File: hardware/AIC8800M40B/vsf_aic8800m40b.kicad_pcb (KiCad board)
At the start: 4 copper layers, 36.8 x 57.2 mm, 86 parts, among them J1 USB_A, J2 USB_C_Receptacle_USB2.0, J3 USB_C_Receptacle_USB2.0, J4 Micro_SD_Card_Det1, J6 Conn_Coaxial, J7 Conn_Coaxial, J8 Conn_01x05, Q1 S9013, SW1 SW_Push, SW2 SW_Push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

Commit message: [hardware/aic8800m40b] update
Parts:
- L4, L5: footprint Inductor_SMD:L_2010_5025Metric -> Inductor_SMD:L_1210_3225Metric
- moved L4 0.89 mm to (216.3, 141.9)
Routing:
- net Net-(U3-SW): track 25.5 -> 9.27 mm
- net Net-(U4-SW): track 14.6 -> 24.8 mm
- net /USB5V_OUT: track 74.5 -> 73.9 mm
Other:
- board text added: "CHIP_BOOT USB_BOOT LINUX_BOOT LINUX/APP"
- board text removed: "CHIP_BOOT USB_BOOT LINUX_BOOT"

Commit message: [hardware/aic8800m40b] update footprint of L1 to be 0805
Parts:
- L1: footprint Inductor_SMD:L_0603_1608Metric -> Inductor_SMD:L_0805_2012Metric
- moved L1 0.51 mm to (226.8, 111.4)
- moved C8 0.10 mm to (229.3, 111.4), turned to -90 degrees
- moved C9 0.10 mm to (226.9, 109.9)
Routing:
- net Net-(U1-V_RF): track 17.8 -> 22.3 mm
- net GND: track 328.9 -> 324.5 mm, vias 206 -> 205
- net /V_CORE: track 10.9 -> 14.8 mm
- net /PWR_3V3: track 137.2 -> 138.8 mm
- net Net-(U1-SW): track 8.21 -> 8.88 mm
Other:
- board text added: "CLK"
- board text added: "DIO"
- board text added: "GND"
- board text added: "RST"
- board text added: "VCC"

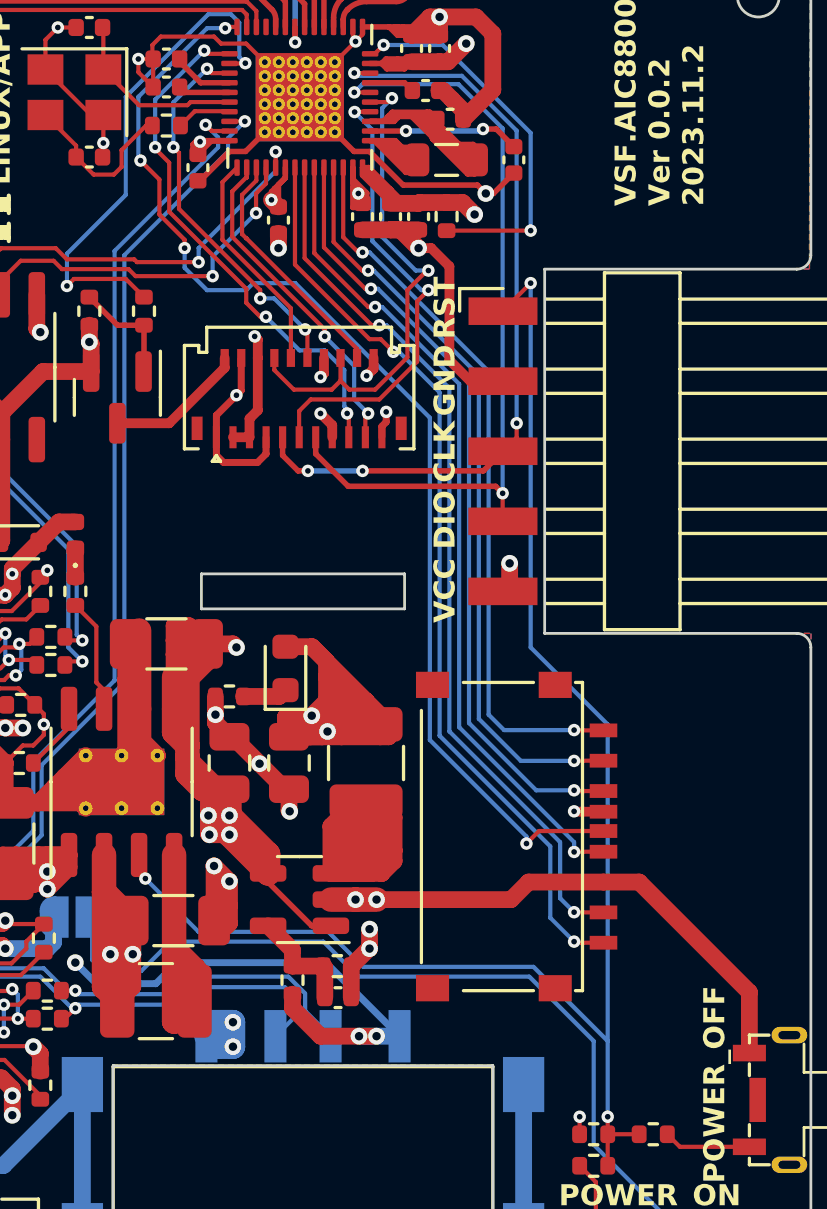
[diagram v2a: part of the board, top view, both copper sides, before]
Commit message: [hardware/aic8800m40b] add test points
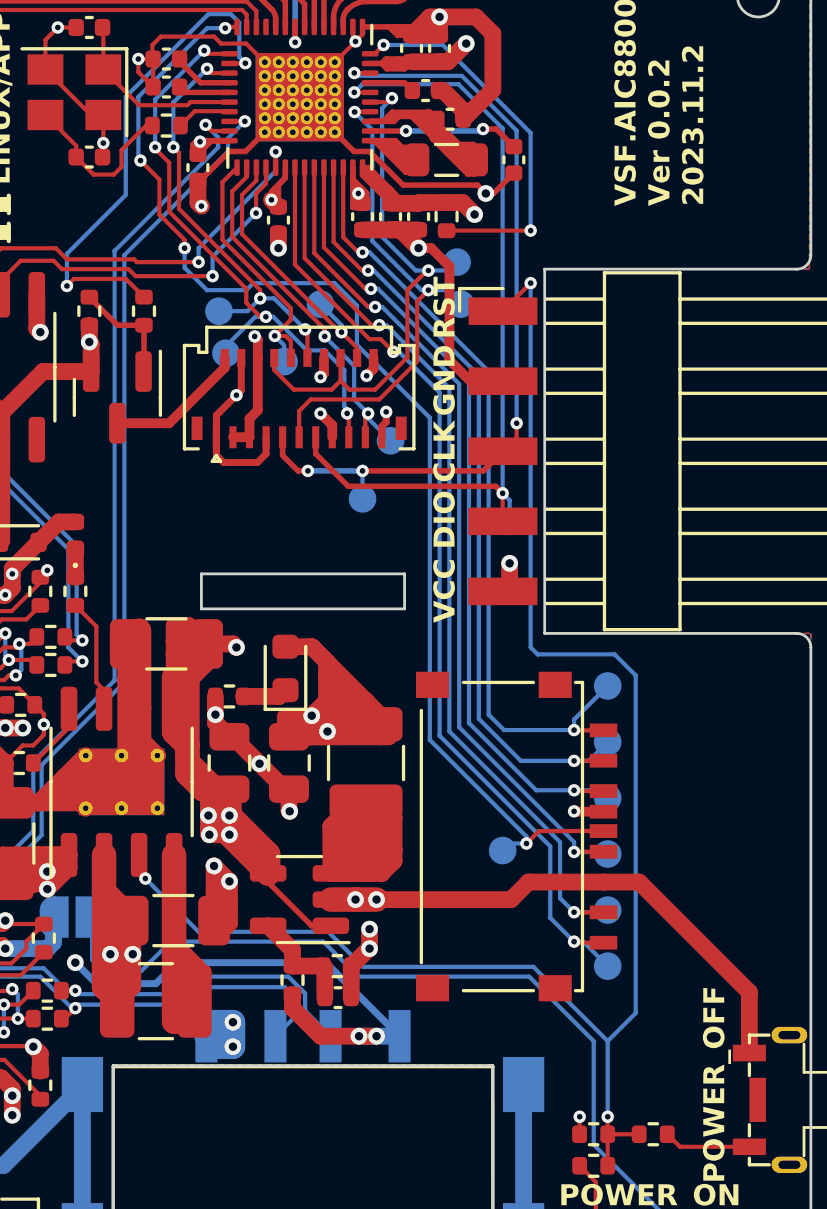
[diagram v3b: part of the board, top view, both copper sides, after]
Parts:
- added TP1: TestPoint, TestPoint:TestPoint_Pad_D1.0mm, B.Cu at (228.9, 136.4)
- added TP10: TestPoint, TestPoint:TestPoint_Pad_D1.0mm, B.Cu at (224.8, 121.5)
- added TP11: TestPoint, TestPoint:TestPoint_Pad_D1.0mm, B.Cu at (222.2, 116.6)
- added TP12: TestPoint, TestPoint:TestPoint_Pad_D1.0mm, B.Cu at (218.8, 118.4)
- added TP13: TestPoint, TestPoint:TestPoint_Pad_D1.0mm, B.Cu at (227.2, 115.1)
- added TP14: TestPoint, TestPoint:TestPoint_Pad_D1.0mm, B.Cu at (229.1, 124.5)
- added TP15: TestPoint, TestPoint:TestPoint_Pad_D1.0mm, B.Cu at (218.6, 116.8)
- added TP16: TestPoint, TestPoint:TestPoint_Pad_D1.0mm, B.Cu at (227.3, 116.6)
- added TP17: TestPoint, TestPoint:TestPoint_Pad_D1.0mm, B.Cu at (220.9, 118.7)
- added TP18: TestPoint, TestPoint:TestPoint_Pad_D1.0mm, B.Cu at (223.8, 123.6)
- added TP2: TestPoint, TestPoint:TestPoint_Pad_D1.0mm, B.Cu at (232.7, 136.5)
- added TP3: TestPoint, TestPoint:TestPoint_Pad_D1.0mm, B.Cu at (232.7, 134.5)
- added TP4: TestPoint, TestPoint:TestPoint_Pad_D1.0mm, B.Cu at (232.7, 138.6)
- added TP5: TestPoint, TestPoint:TestPoint_Pad_D1.0mm, B.Cu at (232.7, 140.6)
- added TP6: TestPoint, TestPoint:TestPoint_Pad_D1.0mm, B.Cu at (232.7, 130.4)
- added TP7: TestPoint, TestPoint:TestPoint_Pad_D1.0mm, B.Cu at (232.7, 132.5)
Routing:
- net GND: track 324.5 -> 329.7 mm, vias 205 -> 206
- net /PWREN: track 55.9 -> 58.4 mm
- net /GPIOB3: track 19.3 -> 21.4 mm
- net /GPIOA10: track 26.7 -> 28.8 mm
- net /GPIOB2: track 42.7 -> 44.6 mm
- net /GPIOA5: track 8.15 -> 9.94 mm, vias 0 -> 1
- net /GPIOA4: track 14.2 -> 15.9 mm
- net /GPIOA15: track 33.7 -> 35.3 mm
- net /GPIOA11: track 27.6 -> 29.1 mm
- net /GPIOA3: track 17.0 -> 18.4 mm
- net /GPIOA7: track 8.85 -> 10.2 mm, vias 0 -> 1
- net /GPIOA12: track 28.5 -> 29.8 mm
- net /GPIOA6: track 12.1 -> 13.4 mm
- net /GPIOA14: track 32.4 -> 33.7 mm
- net /GPIOA13: track 30.1 -> 31.3 mm
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
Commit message: [hardware/aic8800m40b] update modes
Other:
- board text added: "CHIP_BOOT LINUX_BOOT USB_WIFI LINUX/APP"
- board text removed: "CHIP_BOOT USB_BOOT LINUX_BOOT LINUX/APP"
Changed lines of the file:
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@@
     (effects (font (size 0.762 0.762) (thickness 0.1524) bold) (justify left bottom))
   )
-  (gr_text "CHIP_BOOT\nUSB_BOOT\nLINUX_BOOT\nLINUX/APP" (at 211.074 112.268 90) (layer "F.SilkS")
+  (gr_text "CHIP_BOOT\nLINUX_BOOT\nUSB_WIFI\nLINUX/APP" (at 211.074 112.268 90) (layer "F.SilkS")
     (effects (font (size 0.762 0.762) (thickness 0.1524) bold) (justify left bottom))
   )

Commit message: [hardware/aic8800m40b] update silks
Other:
- board text added: "UART PWRIN"
- board text added: "USB PWRIN"
- board text added: "USB PWROUT"
- board text added: "VSF.AIC8800MX0 Ver 0.0.3 2023.12.1"
- board text removed: "VSF.AIC8800MX0 Ver 0.0.2 2023.11.2"
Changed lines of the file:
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@@
     (effects (font (size 0.762 0.762) (thickness 0.1524) bold) (justify left bottom))
   )
-  (gr_text "VSF.AIC8800MX0\nVer 0.0.2\n2023.11.2" (at 236.22 113.03 90) (layer "F.SilkS")
+  (gr_text "VSF.AIC8800MX0\nVer 0.0.3\n2023.12.1" (at 236.22 113.03 90) (layer "F.SilkS")
     (effects (font (size 0.762 0.762) (thickness 0.1524) bold) (justify left bottom))
   )
   (gr_text "CLK" (at 227.203 123.063 90) (layer "F.SilkS")
+    (effects (font (size 0.762 0.762) (thickness 0.1524) bold) (justify left bottom))
+  )
+  (gr_text "USB\nPWROUT" (at 228.727 145.288) (layer "F.SilkS")
     (effects (font (size 0.762 0.762) (thickness 0.1524) bold) (justify left bottom))
   )
@@
     (effects (font (size 0.762 0.762) (thickness 0.1524) bold) (justify left bottom))
   )
+  (gr_text "USB\nPWRIN" (at 210.312 148.59) (layer "F.SilkS")
+    (effects (font (size 0.762 0.762) (thickness 0.1524) bold) (justify left bottom))
+  )
   (gr_text "DIO" (at 227.203 125.476 90) (layer "F.SilkS")
     (effects (font (size 0.762 0.762) (thickness 0.1524) bold) (justify left bottom))
   )
+  (gr_text "UART\nPWRIN" (at 203.581 123.19) (layer "F.SilkS")
+    (effects (font (size 0.762 0.762) (thickness 0.1524) bold) (justify left bottom))
+  )

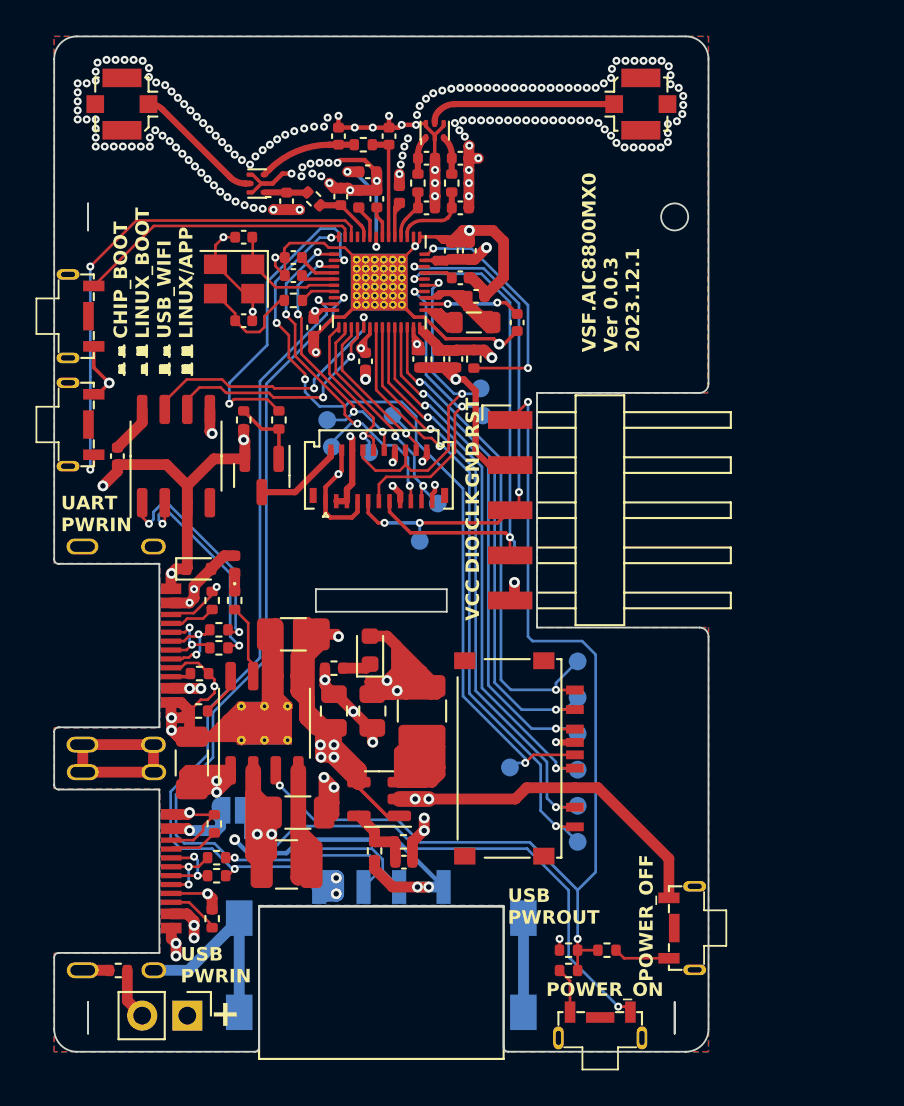
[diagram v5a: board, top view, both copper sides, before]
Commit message: [hardware/aic8800m40b] update to add 2.54 ext port
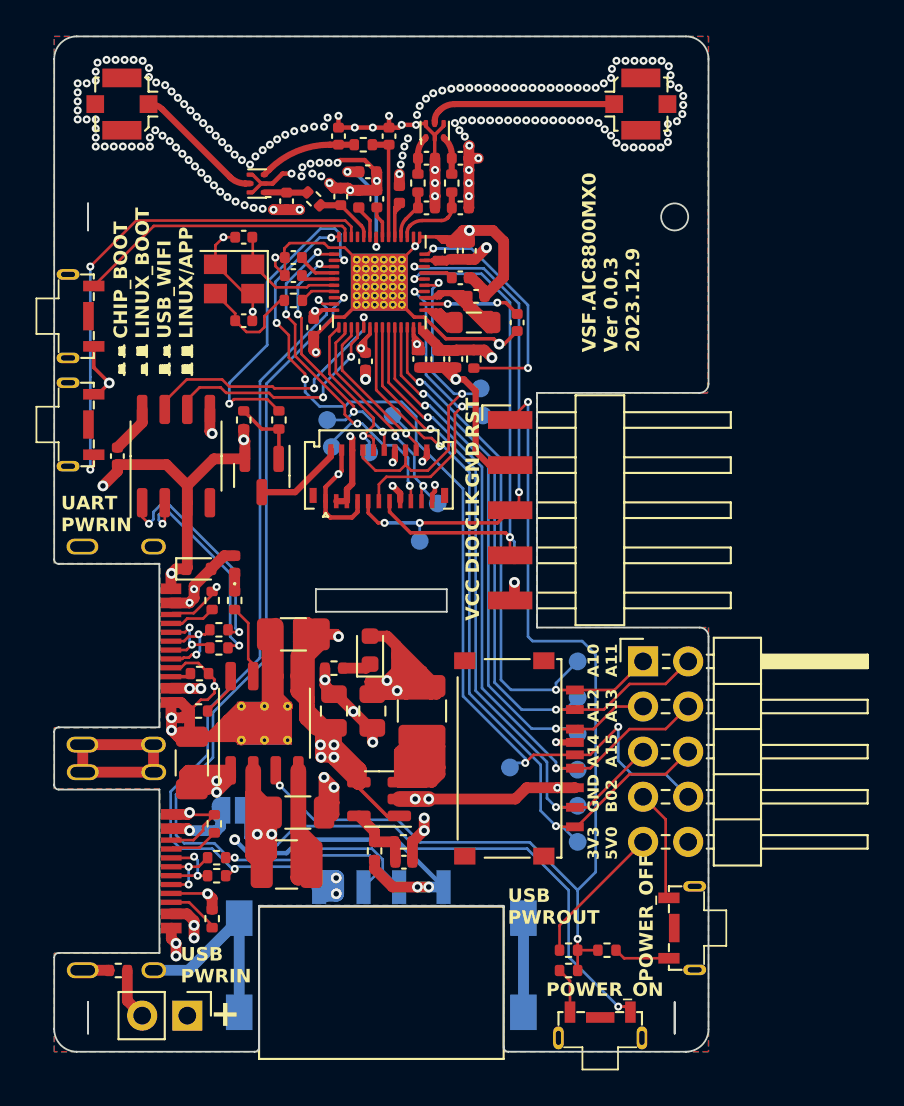
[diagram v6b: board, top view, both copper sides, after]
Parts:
- added J9: Conn_02x05_Odd_Even, Connector_PinHeader_2.54mm:PinHeader_2x05_P2.54mm_Horizontal, F.Cu at (236.3, 130.4)
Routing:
- net /USB5V_OUT: track 73.9 -> 95.3 mm
- net /PWR_3V3: track 138.8 -> 149.9 mm, vias 12 -> 11
- net /GPIOB2: track 44.6 -> 54.3 mm, vias 4 -> 5
- net /GPIOA15: track 35.3 -> 43.4 mm
- net /GPIOA13: track 31.3 -> 39.1 mm
- net /GPIOA11: track 29.1 -> 36.6 mm
- net /GPIOA14: track 33.7 -> 38.8 mm
- net /GPIOA10: track 28.8 -> 33.3 mm
- net /GPIOA12: track 29.8 -> 34.2 mm
- net GND: track 329.7 -> 331.8 mm, vias 206 -> 207
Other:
- board text added: "3V3 5V0"
- board text added: "A10 A11"
- board text added: "A12 A13"
- board text added: "A14 A15"
- board text added: "GND B02"
- board text added: "VSF.AIC8800MX0 Ver 0.0.3 2023.12.9"
- board text removed: "VSF.AIC8800MX0 Ver 0.0.3 2023.12.1"

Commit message: [hardware/aic8800m40b] add connector for all GPIOs
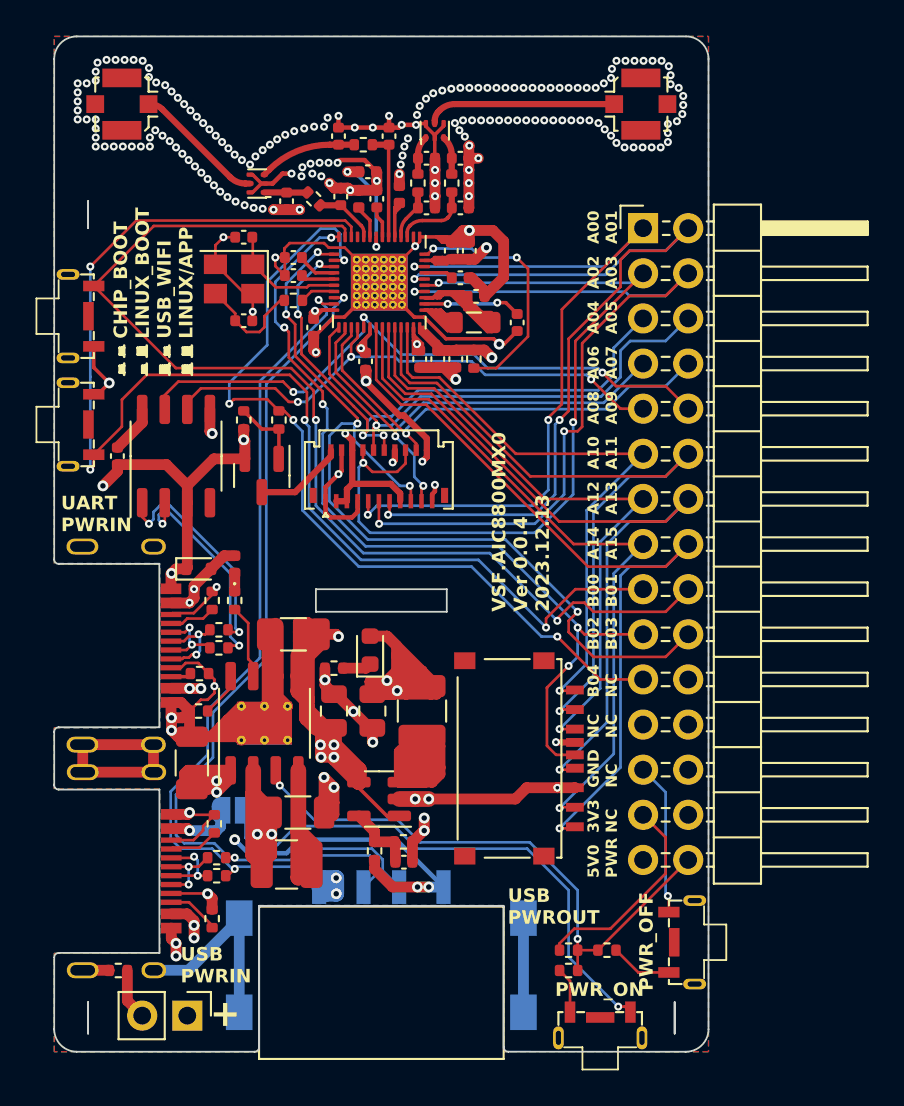
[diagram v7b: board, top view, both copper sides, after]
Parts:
- removed J9: Conn_02x05_Odd_Even, Connector_PinHeader_2.54mm:PinHeader_2x05_P2.54mm_Horizontal
- removed TP1, TP10, TP11, TP12, TP13, TP14, TP15, TP16, TP17, TP18, TP2, TP3, TP4, TP5, TP6, TP7: TestPoint, TestPoint:TestPoint_Pad_D1.0mm
- J8: value Conn_01x05 -> Conn_02x15_Odd_Even; footprint Connector_Harwin:Harwin_M20-89005xx_1x05_P2.54mm_Horizontal -> Connector_PinHeader_2.54mm:PinHeader_2x15_P2.54mm_Horizontal
- moved J8 16.0 mm to (236.3, 106.0)
- moved SW2 0.80 mm to (237.8, 146.2)
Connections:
- net /USB5V renamed /USB5V_IN
- J8 pad 1: /PWREN -> /GPIOA0
- J8 pad 2: GND -> /GPIOA1
- J8 pad 3: /GPIOA0 -> /GPIOA2
- J8 pad 4: /GPIOA1 -> /GPIOA3
- J8 pad 5: /PWR_3V3 -> /GPIOA4
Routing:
- net /GPIOB1: track 16.1 -> 62.3 mm, vias 0 -> 2
- net /GPIOB0: track 28.9 -> 73.5 mm, vias 2 -> 4
- net /GPIOB4: track 18.5 -> 48.0 mm, vias 2 -> 4
- net /GPIOB3: track 21.4 -> 50.4 mm, vias 4 -> 5
- net /GPIOA2: track 20.0 -> 47.7 mm, vias 2 -> 3
- net /GPIOA3: track 18.4 -> 45.9 mm, vias 2 -> 3
- net /PWREN: track 58.4 -> 33.1 mm, vias 3 -> 2
- net /GPIOA9: track 15.3 -> 35.7 mm, vias 2 -> 3
- net /GPIOA5: track 9.94 -> 29.2 mm
- net /GPIOA4: track 15.9 -> 34.5 mm
- net /GPIOA8: track 13.4 -> 30.8 mm, vias 2 -> 3
- net /GPIOA1: track 30.1 -> 47.1 mm, vias 2 -> 3
- net /GPIOA7: track 10.2 -> 26.5 mm
- net /GPIOA6: track 13.4 -> 27.9 mm
- net /GPIOA0: track 29.4 -> 42.8 mm, vias 4 -> 3
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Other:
- outline, holes or cut-outs redrawn
- board text added: "3V3 NC"
- board text added: "5V0 PWR"
- board text added: "A00 A01"
- board text added: "A02 A03"
- board text added: "A04 A05"
- board text added: "A06 A07"
- board text added: "A08 A09"
- board text added: "B00 B01"
- board text added: "B02 B03"
- board text added: "B04 NC"
- board text added: "GND NC"
- board text added: "NC NC"
- board text added: "PWR_OFF"
- board text added: "PWR_ON"
- board text added: "VSF.AIC8800MX0 Ver 0.0.4 2023.12.13"
- board text removed: "3V3 5V0"
- board text removed: "CLK"
- board text removed: "DIO"
- board text removed: "GND"
- board text removed: "GND B02"
- board text removed: "POWER_OFF"
- board text removed: "POWER_ON"
- board text removed: "RST"
- board text removed: "VCC"
- board text removed: "VSF.AIC8800MX0 Ver 0.0.3 2023.12.9"

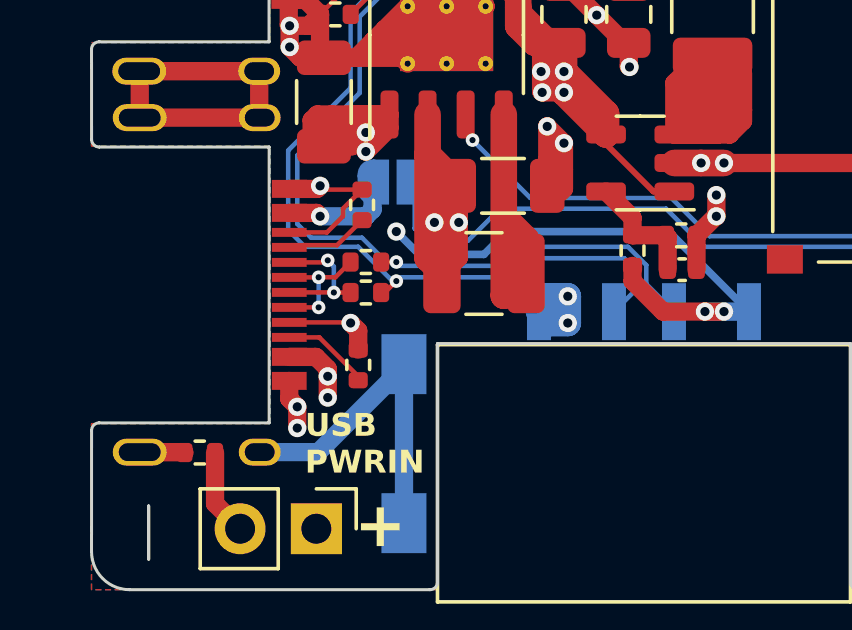
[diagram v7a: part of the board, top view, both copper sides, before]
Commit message: [hardware/aic8800m40b] fix USB-A signals
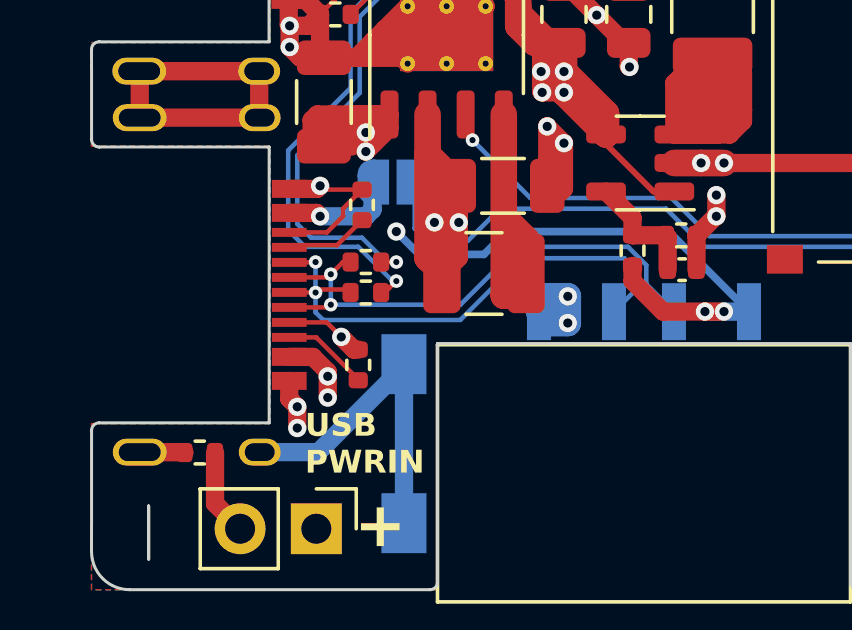
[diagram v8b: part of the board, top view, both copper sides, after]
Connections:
- J1 pad 2: /USB_DM -> /_USB_DM
- J1 pad 3: /USB_DP -> /_USB_DP
- J2 pad A6: Net-(J2-D+-PadA6) -> /_USB_DP
- J2 pad A7: Net-(J2-D--PadA7) -> /_USB_DM
- J2 pad B6: Net-(J2-D+-PadA6) -> /_USB_DP
- J2 pad B7: Net-(J2-D--PadA7) -> /_USB_DM
- R8 pad 2: Net-(J2-D--PadA7) -> /_USB_DM
- R9 pad 2: Net-(J2-D+-PadA6) -> /_USB_DP
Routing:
- net /_USB_DM: track 0.00 -> 18.3 mm, vias 0 -> 2
- net /_USB_DP: track 0.00 -> 18.2 mm, vias 0 -> 2
- net /USB_DP: track 49.9 -> 39.1 mm
- net /USB_DM: track 50.4 -> 40.2 mm
- net Net-(J2-D--PadA7): track 4.51 -> 0.00 mm, vias 2 -> 0
- net Net-(J2-D+-PadA6): track 4.24 -> 0.00 mm, vias 2 -> 0
